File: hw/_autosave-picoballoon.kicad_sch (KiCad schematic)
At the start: 101 parts, among them J1 SOLAR+, J2 SOLAR-, J3 USB_B_Micro, Q1 AO3401A, Q2 AO3401A, Q3 DTC143ZEBTL, Q4 DTC143ZEBTL, Q5 AO3401A, Q6 AO3401A, U1 SPV1040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

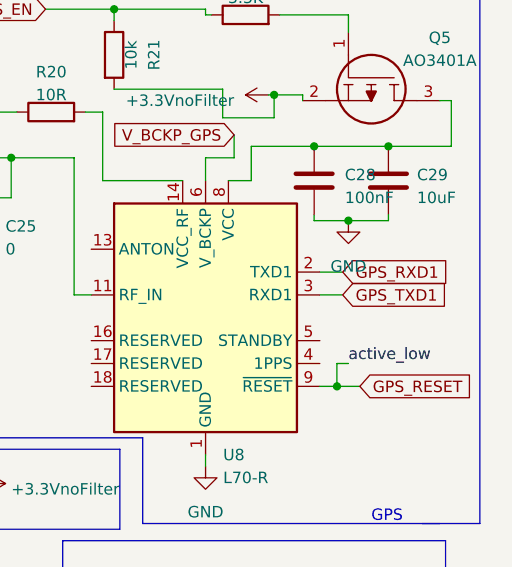
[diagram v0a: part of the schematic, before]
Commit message: Added pinout and fixed wiring GPS TX/RX was wrongly connected. Added conditional compiling for that and fixed schematic only.
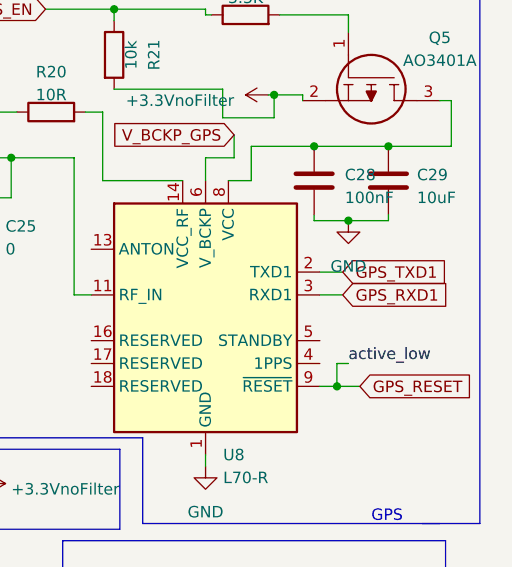
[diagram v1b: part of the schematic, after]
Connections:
- net GPS_RXD1: now also U8.3 (RXD1); no longer U8.2 (TXD1)
- net GPS_TXD1: now also U8.2 (TXD1); no longer U8.3 (RXD1)
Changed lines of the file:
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@@
     )
   )
-  (global_label "GPS_TXD1" (shape input) (at 269.875 47.625 0) (fields_autoplaced)
+  (global_label "GPS_RXD1" (shape input) (at 269.875 47.625 0) (fields_autoplaced)
     (effects (font (size 1.27 1.27)) (justify left))
-    (property "Intersheetrefs" "${INTERSHEET_REFS}" (at 282.1545 47.625 0)
+    (property "Intersheetrefs" "${INTERSHEET_REFS}" (at 282.5363 47.625 0)
       (effects (font (size 1.27 1.27)) (justify left) hide)
     )
@@
     )
   )
-  (global_label "GPS_RXD1" (shape input) (at 269.875 45.085 0) (fields_autoplaced)
+  (global_label "GPS_TXD1" (shape input) (at 269.875 45.085 0) (fields_autoplaced)
     (effects (font (size 1.27 1.27)) (justify left))
-    (property "Intersheetrefs" "${INTERSHEET_REFS}" (at 282.4569 45.085 0)
+    (property "Intersheetrefs" "${INTERSHEET_REFS}" (at 282.2339 45.085 0)
       (effects (font (size 1.27 1.27)) (justify left) hide)
     )
